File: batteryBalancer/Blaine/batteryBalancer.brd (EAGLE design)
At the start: 101.6 x 101.6 mm, 31 parts

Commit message: Added net names
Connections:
- net N$1 renamed BALANCED_INDICATOR
- net N$10 renamed PORT_INDICATOR
- net N$11 renamed ADC_A0
- net N$12 renamed KILL_SWITCH
- net N$13 renamed ADC_A1
- net N$14 renamed PORT_UNBALANCED
- net N$15 renamed OFF
- net N$16 renamed STBD_UNBALANCED
- net N$17 renamed SCL
- net N$19 renamed PORT_POWER
- net N$2 renamed STBD_GATE
- net N$20 renamed STBD_FUSED
- net N$22 renamed MOTOR_POWER2
- net N$24 renamed PORT_CURRENT
- net N$25 renamed STBD_CURRENT
- net N$3 renamed BALANCED_POWER
- net N$4 renamed STBD_POWER
- net N$5 renamed MOTOR_POWER1
- net N$6 renamed PORT_GATE
- net N$7 renamed PORT_FUSED
- net N$8 renamed STBD_INDICATOR
- net N$9 renamed SDA
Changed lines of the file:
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@@
 <wire x1="131.191" y1="-18.3007" x2="127" y2="-18.3007" width="0" layer="19" extent="1-1"/>
 </signal>
-<signal name="N$2">
+<signal name="STBD_GATE">
 <contactref element="STBD_FC" pad="5"/>
 <contactref element="STBD_FET" pad="GATE"/>
 <wire x1="20.3835" y1="-20.6375" x2="31.75" y2="-239.9999" width="0" layer="19" extent="1-1"/>
 </signal>
-<signal name="N$6">
+<signal name="PORT_GATE">
 <contactref element="PORT_FC" pad="5"/>
 <contactref element="PORT_FET" pad="GATE"/>
 <wire x1="72.771" y1="-20.6375" x2="26.9875" y2="-239.9999" width="0" layer="19" extent="1-1"/>
 </signal>
-<signal name="N$8">
+<signal name="STBD_INDICATOR">
 <contactref element="R2" pad="2"/>
 <contactref element="STBD_STATUS" pad="CATHODE"/>
 <wire x1="76.7875" y1="-238.125" x2="42.775" y2="-239.7125" width="0" layer="19" extent="1-1"/>
 </signal>
-<signal name="N$1">
+<signal name="BALANCED_INDICATOR">
 <contactref element="R3" pad="1"/>
 <contactref element="BALANCED_STATUS" pad="ANODE"/>
@@
 <wire x1="24.1455" y1="3.175" x2="26.6855" y2="3.175" width="0" layer="19" extent="1-1"/>
 </signal>
-<signal name="N$14">
+<signal name="PORT_UNBALANCED">
 <contactref element="PORT_FC" pad="4"/>
 <contactref element="PORT_FET" pad="SOURCE"/>
@@
 <wire x1="83.566" y1="-20.6375" x2="27.9375" y2="-239.9999" width="0" layer="19" extent="1-1"/>
 </signal>
-<signal name="N$16">
+<signal name="STBD_UNBALANCED">
 <contactref element="STBD_FET" pad="SOURCE"/>
 <contactref element="STBD_FC" pad="4"/>
@@
 <wire x1="31.1785" y1="-20.6375" x2="32.7" y2="-239.9999" width="0" layer="19" extent="1-1"/>
 </signal>
-<signal name="N$17">
+<signal name="SCL">
 <contactref element="ADC" pad="SCL"/>
 <contactref element="EDGE_CONNECTOR" pad="SCL_SENSOR"/>
@@
 <wire x1="21.6055" y1="3.175" x2="19.0655" y2="3.175" width="0" layer="19" extent="1-1"/>
 </signal>
-<signal name="N$11">
+<signal name="ADC_A0">
 <contactref element="R4" pad="1"/>
 <contactref element="ADC" pad="A0"/>
@@
 <wire x1="61.825" y1="-239.7125" x2="49.3" y2="-239.7125" width="0" layer="19" extent="1-1"/>
 </signal>
-<signal name="N$13">
+<signal name="ADC_A1">
 <contactref element="ADC" pad="A1"/>
 <contactref element="R7" pad="2"/>
@@
 <wire x1="66.5875" y1="-239.7125" x2="54.0625" y2="-239.7125" width="0" layer="19" extent="1-1"/>
 </signal>
-<signal name="N$20">
+<signal name="STBD_FUSED">
 <contactref element="STBD_CS" pad="IP+1"/>
 <contactref element="STBD_CS" pad="IP+2"/>
@@
 <wire x1="98.7425" y1="-103.1875" x2="91.1225" y2="-103.1875" width="0" layer="19" extent="1-1"/>
 </signal>
-<signal name="N$24">
+<signal name="PORT_CURRENT">
 <contactref element="PORT_CS" pad="VIOUT"/>
 <contactref element="ADC" pad="IN0"/>
 <wire x1="20.3375" y1="-240.6125" x2="8.89" y2="-240.2713" width="0" layer="19" extent="1-1"/>
 </signal>
-<signal name="N$25">
+<signal name="STBD_CURRENT">
 <contactref element="STBD_CS" pad="VIOUT"/>
 <contactref element="ADC" pad="IN1"/>
 <wire x1="20.3375" y1="-241.2625" x2="2.54" y2="-240.2713" width="0" layer="19" extent="1-1"/>
 </signal>
-<signal name="N$4">
+<signal name="STBD_POWER">
 <contactref element="BATTERY_STBD" pad="3"/>
 <contactref element="BATTERY_STBD" pad="2"/>
@@
 <wire x1="62.484" y1="-65.0875" x2="66.675" y2="-65.0875" width="0" layer="19" extent="1-1"/>
 </signal>
-<signal name="N$19">
+<signal name="PORT_POWER">
 <contactref element="PORT_FUSE" pad="P$2"/>
 <contactref element="PORT_FUSE" pad="P$1"/>
@@
 <wire x1="18.034" y1="-65.0875" x2="22.225" y2="-65.0875" width="0" layer="19" extent="1-1"/>
 </signal>
-<signal name="N$3">
+<signal name="BALANCED_POWER">
 <contactref element="BATTERY_BALANCED" pad="3"/>
 <contactref element="BATTERY_BALANCED" pad="2"/>
@@
 <wire x1="25.7175" y1="-20.6375" x2="78.105" y2="-20.6375" width="0" layer="19" extent="1-1"/>
 </signal>
-<signal name="N$5">
+<signal name="MOTOR_POWER1">
 <contactref element="RELAY2" pad="LOAD-"/>
 <contactref element="MOTOR_POWER1" pad="3"/>
@@
 <wire x1="106.934" y1="-65.0875" x2="111.125" y2="-65.0875" width="0" layer="19" extent="1-1"/>
 </signal>
-<signal name="N$22">
+<signal name="MOTOR_POWER2">
 <contactref element="RELAY3" pad="LOAD-"/>
 <contactref element="MOTOR_POWER2" pad="2"/>
@@
 <wire x1="18.034" y1="-106.3625" x2="22.225" y2="-106.3625" width="0" layer="19" extent="1-1"/>
 </signal>
-<signal name="N$7">
+<signal name="PORT_FUSED">
 <contactref element="PORT_FUSE" pad="P$4"/>
 <contactref element="PORT_FUSE" pad="P$3"/>
@@
 <wire x1="46.6725" y1="-144.4625" x2="54.2925" y2="-144.4625" width="0" layer="19" extent="1-1"/>
 </signal>
-<signal name="N$9">
+<signal name="SDA">
 <contactref element="EDGE_CONNECTOR" pad="SDA_SENSOR"/>
 <contactref element="ADC" pad="SDA"/>
 <wire x1="77.4855" y1="3.175" x2="14.5875" y2="-241.2625" width="0" layer="19" extent="1-1"/>
 </signal>
-<signal name="N$12">
+<signal name="KILL_SWITCH">
 <contactref element="RLAY1" pad="CONTROL+"/>
 <contactref element="RELAY4" pad="CONTROL+"/>
@@
 <wire x1="64.7855" y1="3.175" x2="97.4925" y2="-142.875" width="0" layer="19" extent="1-1"/>
 </signal>
-<signal name="N$10">
+<signal name="PORT_INDICATOR">
 <contactref element="R1" pad="2"/>
 <contactref element="PORT_STATUS" pad="CATHODE"/>
 <wire x1="70.4375" y1="-238.125" x2="38.0125" y2="-239.7125" width="0" layer="19" extent="1-1"/>
 </signal>
-<signal name="N$15">
+<signal name="OFF">
 <contactref element="PORT_FC" pad="3"/>
 <contactref element="STBD_FC" pad="3"/>

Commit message: Started board design
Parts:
- added KILL_SWITCH_CONNECTOR: 39-30-02?, con-molex-mini-fit:39-30-?02?
- C1: value 0.1uF -> 22uF
- moved OFF 360.6 mm to (34.5, 98.0), turned to 270 degrees
- moved STBD_CS 333.9 mm to (18.7, 90.6)
- moved R1 329.9 mm to (64.8, 89.0), turned to 270 degrees
- moved STBD_STATUS 329.0 mm to (44.4, 89.2)
- moved R2 328.9 mm to (39.3, 89.2), turned to 270 degrees
- moved PORT_STATUS 327.4 mm to (59.4, 89.1), turned to 180 degrees
- moved STBD_FC 324.7 mm to (64.2, 81.8), turned to 270 degrees
- moved PORT_FC 323.1 mm to (41.7, 81.5), turned to 270 degrees
- moved PORT_CS 315.8 mm to (82.1, 64.5), turned to 180 degrees
- moved R7 312.1 mm to (6.79, 66.9), turned to 90 degrees
- moved R5 309.9 mm to (10.8, 66.9), turned to 270 degrees
- moved R6 305.1 mm to (6.79, 60.7), turned to 270 degrees
- moved ADC 303.4 mm to (19.1, 60.5), turned to 270 degrees
- moved R4 303.1 mm to (10.8, 60.7), turned to 90 degrees
- moved BALANCED_STATUS 298.5 mm to (17.4, 52.9), turned to 270 degrees
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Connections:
- removed net PORT_FUSED: PORT_CS.IP+1, PORT_CS.IP+2, PORT_FUSE.P$3, PORT_FUSE.P$4, PORT_STATUS.ANODE
- removed net STBD_FUSED: STBD_CS.IP+1, STBD_CS.IP+2, STBD_FUSE.P$3, STBD_FUSE.P$4, STBD_STATUS.ANODE
- new net N$1: PORT_FC.4, PORT_FET.SOURCE, PORT_FUSE.P$3, PORT_FUSE.P$4, PORT_STATUS.ANODE
- new net N$2: STBD_CS.IP-1, STBD_CS.IP-2, STBD_FUSE.P$1, STBD_FUSE.P$2
- net KILL_SWITCH: now also KILL_SWITCH_CONNECTOR.1
- net LOGIC_GND: now also KILL_SWITCH_CONNECTOR.2
- net PORT_POWER: now also PORT_CS.IP+1, PORT_CS.IP+2; no longer PORT_FUSE.P$1, PORT_FUSE.P$2
- net PORT_UNBALANCED: now also PORT_FUSE.P$1, PORT_FUSE.P$2; no longer PORT_FC.4, PORT_FET.SOURCE
- net STBD_POWER: now also STBD_CS.IP+1, STBD_CS.IP+2; no longer STBD_FUSE.P$1, STBD_FUSE.P$2
- net STBD_UNBALANCED: now also STBD_FUSE.P$3, STBD_FUSE.P$4, STBD_STATUS.ANODE; no longer STBD_CS.IP-1, STBD_CS.IP-2

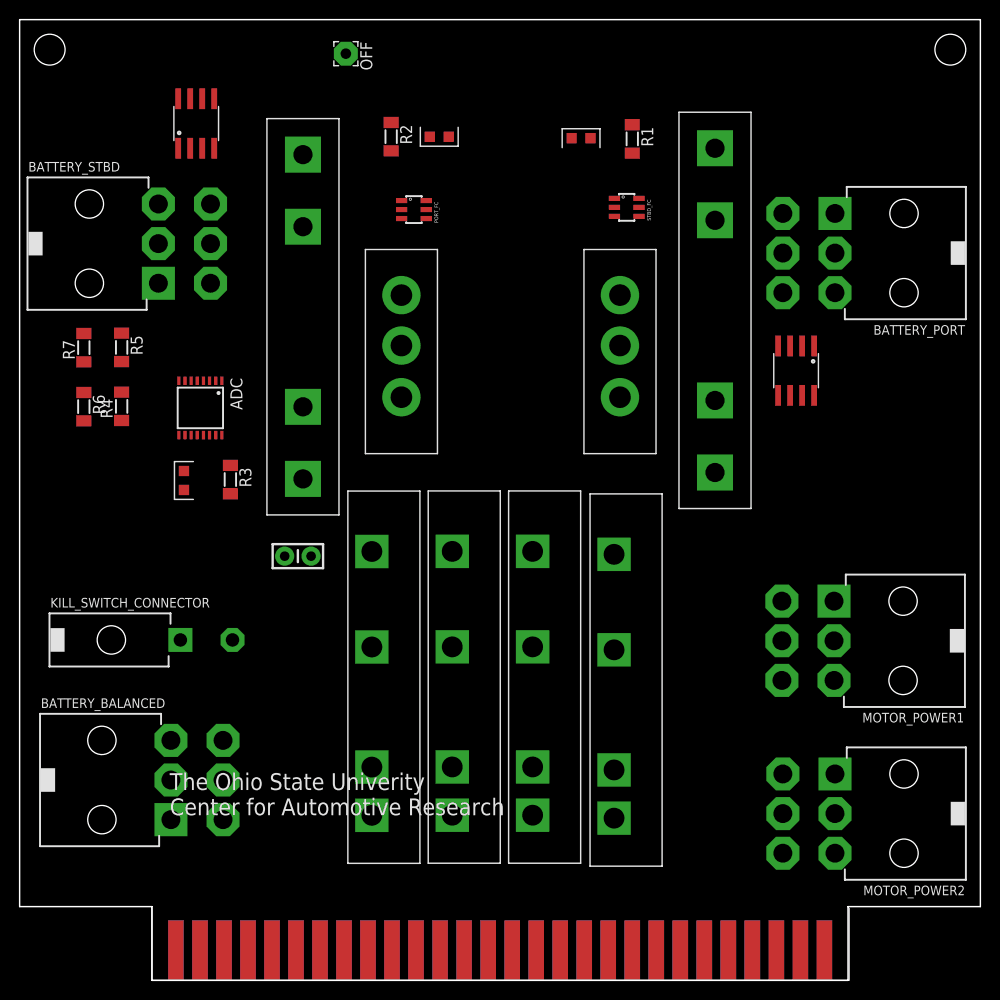
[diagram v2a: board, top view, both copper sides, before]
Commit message: Routed the board
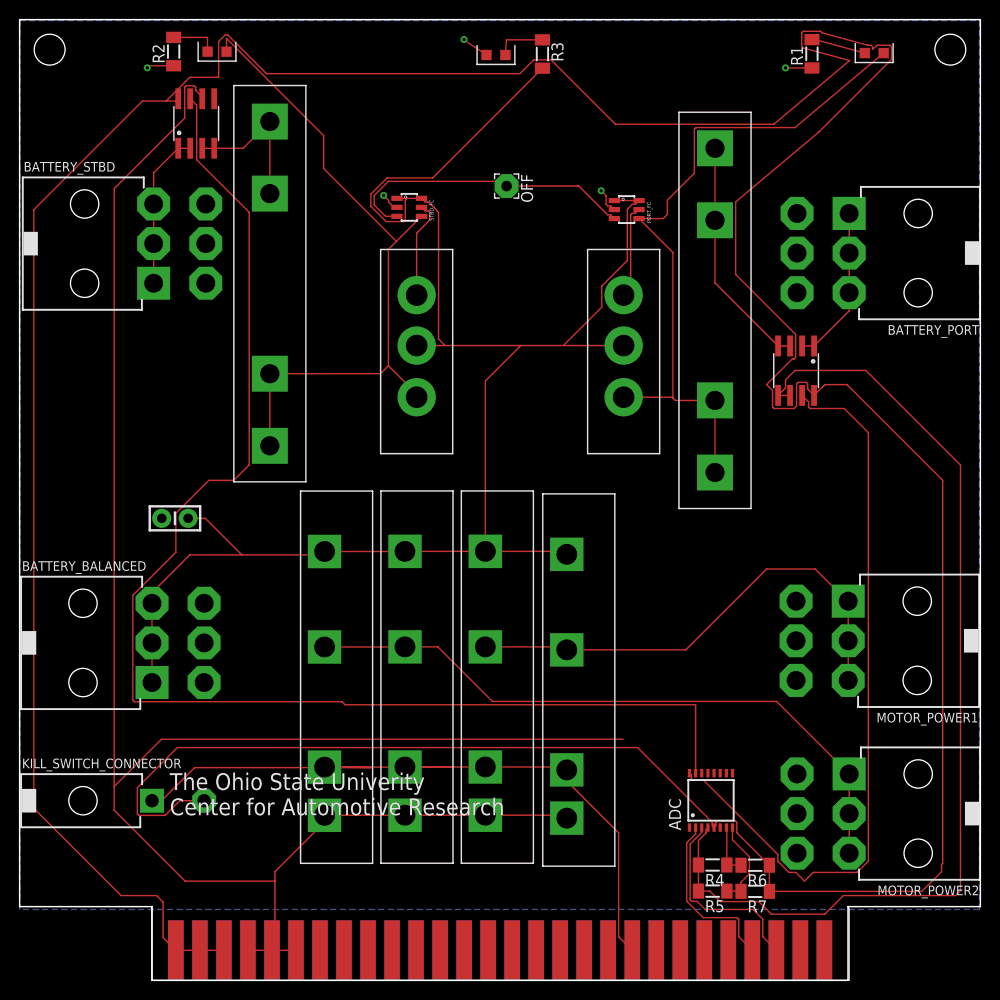
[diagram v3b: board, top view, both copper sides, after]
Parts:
- moved R7 91.4 mm to (77.8, 9.41), turned to 180 degrees
- moved R6 86.0 mm to (77.8, 12.2), turned to 180 degrees
- moved R5 84.9 mm to (73.3, 9.44), turned to 180 degrees
- moved R4 79.1 mm to (73.3, 12.2), turned to 180 degrees
- moved ADC 68.1 mm to (73.1, 19.0), turned to 90 degrees
- moved R3 55.8 mm to (55.3, 98.0)
- moved BALANCED_STATUS 55.8 mm to (50.4, 97.9), turned to 0 degrees
- moved PORT_STATUS 32.3 mm to (90.4, 98.1), turned to 0 degrees
- moved STBD_STATUS 25.2 mm to (20.9, 98.2)
- moved R2 24.7 mm to (16.3, 98.2), turned to 90 degrees
- moved PORT_FET 23.5 mm to (63.9, 65.9)
- moved STBD_FC 23.0 mm to (41.2, 81.8)
- moved PORT_FC 22.5 mm to (64.2, 81.5)
- moved OFF 22.0 mm to (51.5, 84.0)
- moved STBD_FET 21.5 mm to (42.0, 65.9)
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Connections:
- net 3.3V: now also KILL_SWITCH_CONNECTOR.2
- net LOGIC_GND: no longer KILL_SWITCH_CONNECTOR.2
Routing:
- net 3.3V: track 0.00 -> 439.0 mm
- net LOGIC_GND: track 0.00 -> 314.1 mm
- net BALANCED_POWER: track 0.00 -> 181.7 mm
- net STBD_CURRENT: track 0.00 -> 139.8 mm
- net KILL_SWITCH: track 0.00 -> 87.3 mm
- net PORT_CURRENT: track 0.00 -> 79.4 mm
- net N$1: track 0.00 -> 74.4 mm
- net STBD_UNBALANCED: track 0.00 -> 72.6 mm
- net MOTOR_POWER2: track 0.00 -> 69.6 mm
- net MOTOR_POWER1: track 0.00 -> 51.9 mm
- net OFF: track 0.00 -> 31.7 mm
- net PORT_UNBALANCED: track 0.00 -> 24.9 mm
- net SCL: track 0.00 -> 20.6 mm
- net SDA: track 0.00 -> 18.3 mm
- net PORT_POWER: track 0.00 -> 17.1 mm
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- added copper zone on layer 16, net GND

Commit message: Fixed a trace
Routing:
- net LOGIC_GND: track 314.1 -> 328.9 mm, vias 0 -> 2
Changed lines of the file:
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@@
 <layer number="14" name="Route14" color="1" fill="6" visible="no" active="no"/>
 <layer number="15" name="Route15" color="4" fill="6" visible="no" active="no"/>
-<layer number="16" name="Bottom" color="1" fill="1" visible="no" active="yes"/>
+<layer number="16" name="Bottom" color="1" fill="1" visible="yes" active="yes"/>
 <layer number="17" name="Pads" color="2" fill="1" visible="yes" active="yes"/>
 <layer number="18" name="Vias" color="2" fill="1" visible="yes" active="yes"/>
@@
 <contactref element="MOTOR_POWER1" pad="6"/>
 <contactref element="MOTOR_POWER1" pad="5"/>
-<polygon width="0.508" layer="16" isolate="0.3048">
-<vertex x="0" y="101.5"/>
-<vertex x="101.5" y="101.5"/>
-<vertex x="101.5" y="7.5"/>
-<vertex x="0" y="7.5"/>
-</polygon>
 <via x="13.5" y="96.5" extent="1-16" drill="0.35"/>
 <via x="81" y="96.5" extent="1-16" drill="0.35"/>
@@
 <wire x1="49.375" y1="97.8625" x2="47.1375" y2="99.3625" width="0.15" layer="1"/>
 <wire x1="47.1375" y1="99.3625" x2="47" y2="99.5" width="0.15" layer="1"/>
+<polygon width="0.1524" layer="16">
+<vertex x="0" y="101.5"/>
+<vertex x="101.5" y="101.5"/>
+<vertex x="101.5" y="8"/>
+<vertex x="0" y="8"/>
+</polygon>
 </signal>
 <signal name="STBD_GATE">
@@
 <wire x1="10" y1="18" x2="10" y2="20.5" width="0.15" layer="1"/>
 <wire x1="10" y1="20.5" x2="15" y2="25.5" width="0.15" layer="1"/>
-<wire x1="72.5925" y1="16.3575" x2="72.5925" y2="16.72848125" width="0" layer="19" extent="1-16"/>
-<wire x1="72.5925" y1="16.3575" x2="72.7875" y2="16.1625" width="0" layer="19" extent="1-16"/>
 <wire x1="15" y1="25.5" x2="63.82098125" y2="25.5" width="0.15" layer="1"/>
 <wire x1="71.7875" y1="12.2" x2="71.7875" y2="9.4375" width="0.15" layer="1"/>
@@
 <contactref element="STBD_CS" pad="GND"/>
 <contactref element="STBD_CS" pad="BW_SEL"/>
+<wire x1="72.5937" y1="16.728975" x2="72.428975" y2="16.8937" width="0.1524" layer="1"/>
+<wire x1="72.7875" y1="16.1625" x2="72.5937" y2="16.3563" width="0.1524" layer="1"/>
+<wire x1="72.5937" y1="16.3563" x2="72.5937" y2="16.728975" width="0.1524" layer="1"/>
+<wire x1="70.1063" y1="16.8937" x2="72.428975" y2="16.8937" width="0.1524" layer="1"/>
+<via x="66" y="21" extent="1-16" drill="0.35"/>
+<via x="64.5" y="25.5" extent="1-16" drill="0.35"/>
+<wire x1="64.5" y1="25.5" x2="64.5" y2="22.5" width="0.1524" layer="16"/>
+<wire x1="64.5" y1="22.5" x2="66" y2="21" width="0.1524" layer="16"/>
+<wire x1="63.82098125" y1="25.5" x2="64.5" y2="25.5" width="0.1524" layer="1"/>
+<wire x1="66" y1="21" x2="70.1063" y2="16.8937" width="0.1524" layer="1"/>
 <wire x1="19.5" y1="93.2287" x2="20.58" y2="93.2287" width="0" layer="19" extent="1-1"/>
 <wire x1="19.31" y1="93.2287" x2="19.5" y2="93.2287" width="0" layer="19" extent="1-1"/>
-<wire x1="72.5925" y1="16.72848125" x2="63.82098125" y2="25.5" width="0" layer="19" extent="1-1"/>
 </signal>
 <signal name="PORT_UNBALANCED">

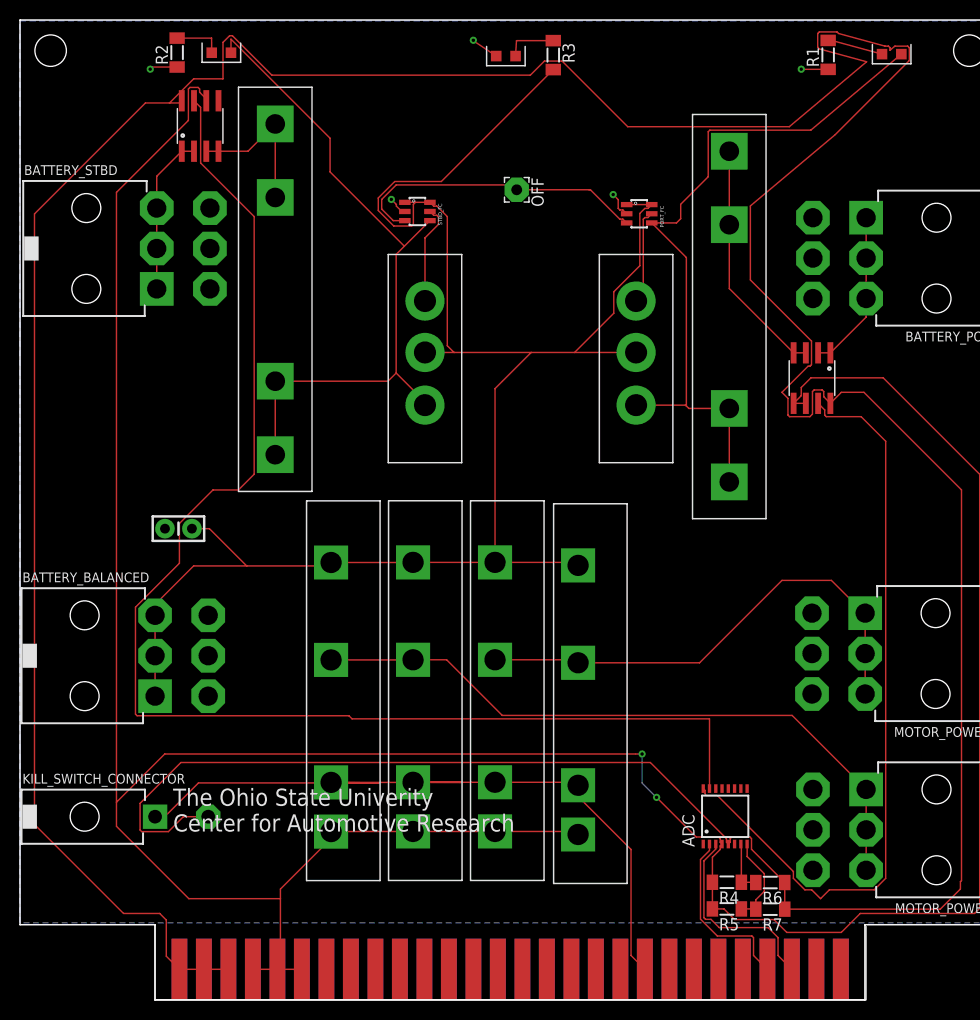
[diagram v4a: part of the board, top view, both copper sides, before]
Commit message: Made traces the right size
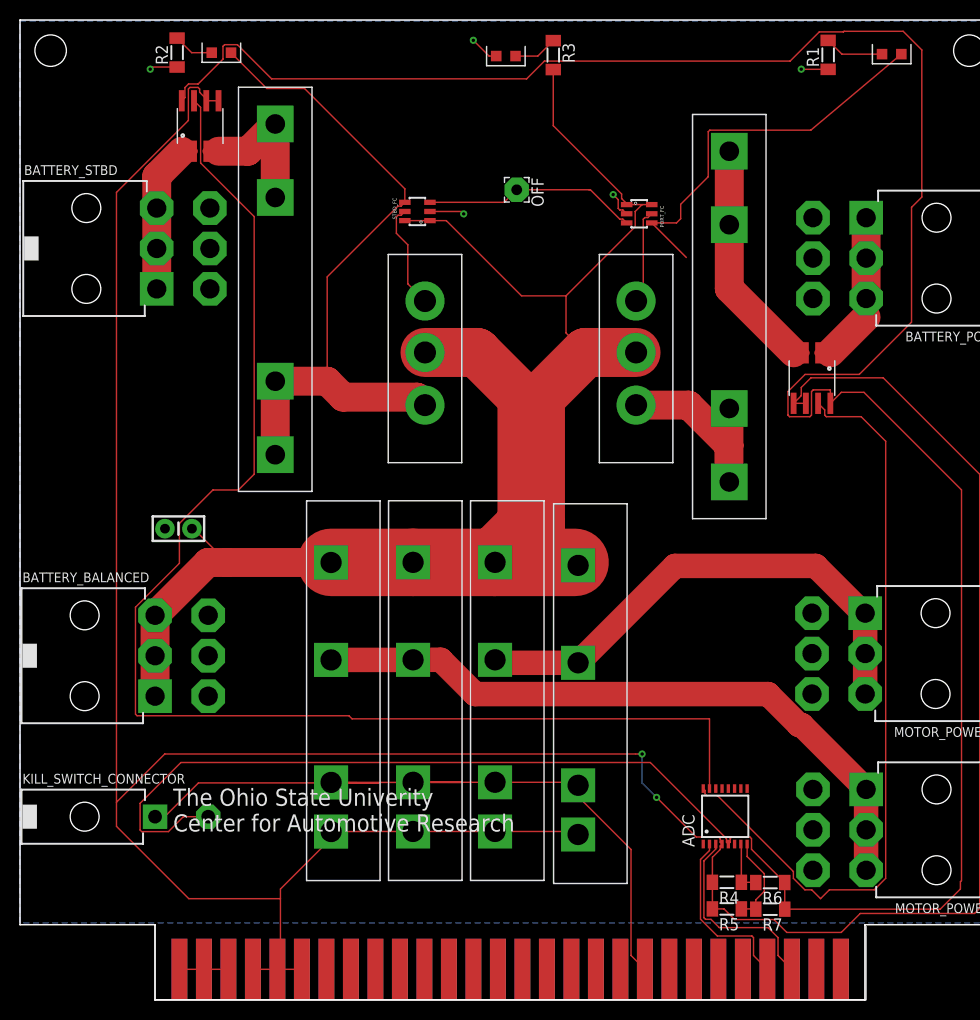
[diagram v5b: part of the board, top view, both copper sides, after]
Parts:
- turned STBD_FC to 90 degrees
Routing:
- net 3.3V: track 439.0 -> 312.8 mm
- net BALANCED_POWER: track 181.7 -> 163.6 mm
- net N$1: track 74.4 -> 60.4 mm
- net OFF: track 31.7 -> 22.5 mm
- net GND: track 13.3 -> 15.1 mm
- net LOGIC_GND: track 328.9 -> 330.2 mm
- net MOTOR_POWER1: track 51.9 -> 53.1 mm
- net STBD_UNBALANCED: track 72.6 -> 71.5 mm
- net STBD_INDICATOR: track 5.09 -> 4.21 mm
- net BALANCED_INDICATOR: track 5.42 -> 4.58 mm
- net STBD_GATE: track 10.4 -> 11.1 mm
